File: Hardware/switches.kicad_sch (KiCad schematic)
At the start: 40 parts, among them J5 Conn_01x02_Male, J6 Conn_01x08_Male, J7 FAN, J8 XT60PW-F, J9 Conn_01x02_Male, Q1 SQS141ELNW-T1_GE3, Q2 SQS141ELNW-T1_GE3, Q3 SI7635DP-T1-GE3, Q4 SI7635DP-T1-GE3, Q5 SSM3K15AMFV,L3F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

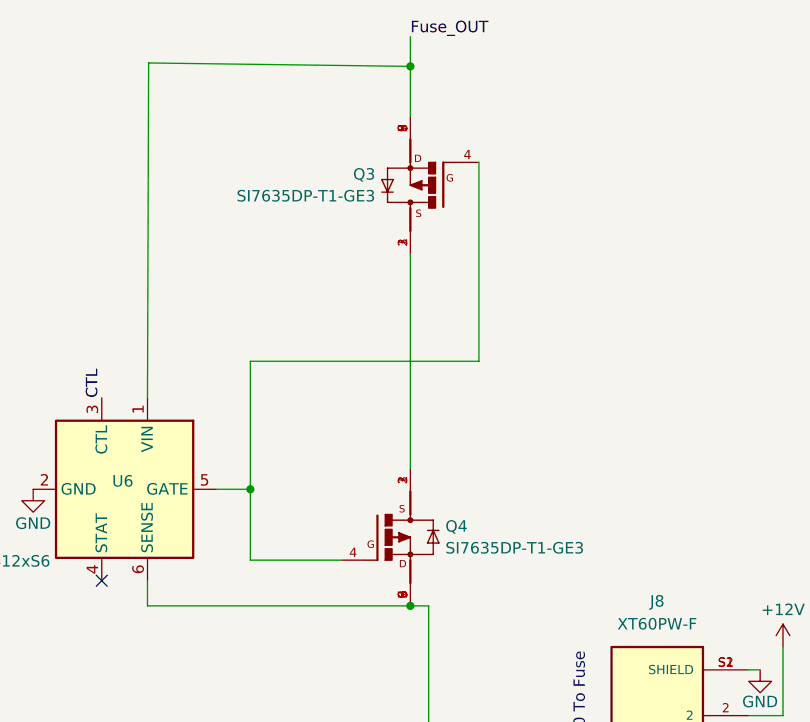
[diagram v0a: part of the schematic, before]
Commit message: feat: Changed mosfet to non deprecated version
Higher input voltage too: SI7135DP-T1-GE3
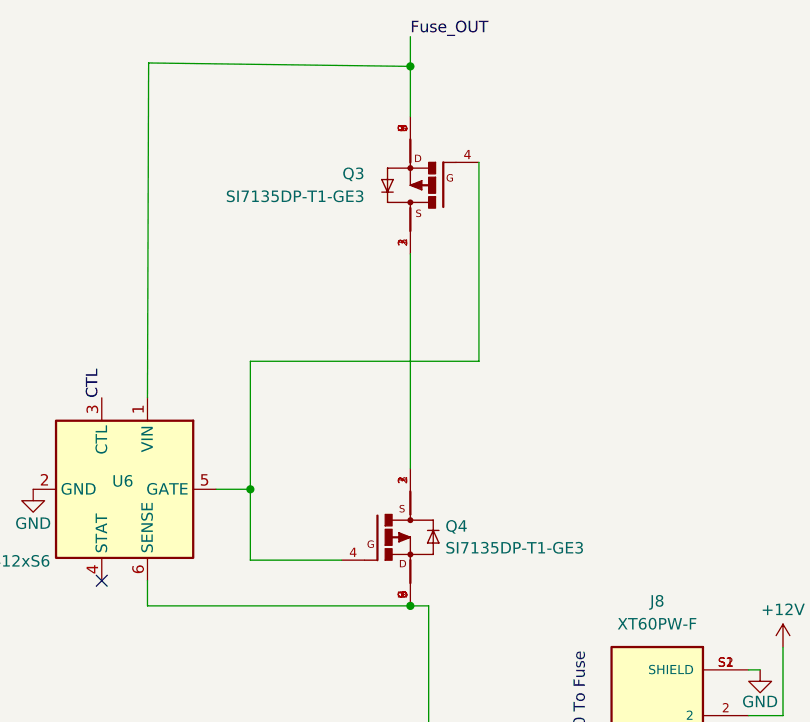
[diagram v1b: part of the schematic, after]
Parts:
- Q3, Q4: value SI7635DP-T1-GE3 -> SI7135DP-T1-GE3; Check_prices https://www.snapeda.com/parts/SI7635DP-T1-GE3/Vishay+Silico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 -> https://www.mouser.co.uk/ProductDetail/Vishay-Semiconductor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; Description_1 P-Channel 20 V 40A (Tc) 5W (Ta), 54W (Tc) Surface Mount Pow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 -> P-Channel 30 V 60A Surface Mount PowerPAK® SO-8; MP SI7635DP-T1-GE3 -> SI7135DP-T1-GE3; SnapEDA_Link https://www.snapeda.com/parts/SI7635DP-T1-GE3/Vishay+Silico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 -> (none)
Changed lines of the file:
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@@
 			)
 		)
-		(property "Value" "SI7635DP-T1-GE3"
+		(property "Value" "SI7135DP-T1-GE3"
 			(at 156.7942 85.5401 0)
 			(effects
@@
 			)
 		)
-		(property "Description_1" "\nP-Channel 20 V 40A (Tc) 5W (Ta), 54W (Tc) Surface Mount PowerPAK® SO-8\n"
+		(property "Description_1" "\nP-Channel 30 V 60A Surface Mount PowerPAK® SO-8\n"
 			(at 152.908 84.328 0)
 			(effects
@@
 			)
 		)
-		(property "Check_prices" "https://www.snapeda.com/parts/SI7635DP-T1-GE3/Vishay+Siliconix/view-part/?ref=eda"
+		(property "Check_prices" "https://www.mouser.co.uk/ProductDetail/Vishay-Semiconductors/SI7135DP-T1-GE3?qs=IRuQNBqMOcnMinMQAFe5cQ%3D%3D"
 			(at 152.908 84.328 0)
 			(effects
@@
 			)
 		)
-		(property "SnapEDA_Link" "https://www.snapeda.com/parts/SI7635DP-T1-GE3/Vishay+Siliconix/view-part/?ref=snap"
+		(property "SnapEDA_Link" ""
 			(at 152.908 84.328 0)
 			(effects
@@
 			)
 		)
-		(property "MP" "SI7635DP-T1-GE3"
+		(property "MP" "SI7135DP-T1-GE3"
 			(at 152.908 84.328 0)
 			(effects
@@
 	)
 	(symbol
-		(lib_id "iclr:SI7635DP-T1-GE3")
-		(at 152.908 45.212 180)
-		(unit 1)
-		(exclude_from_sim no)
-		(in_bom yes)
-		(on_board yes)
-		(dnp no)
-		(fields_autoplaced yes)
-		(property "Reference" "Q3"
-			(at 149.0219 43.9998 0)
-			(effects
-				(font
-					(size 1.27 1.27)
-				)
-				(justify left)
-			)
-		)
-		(property "Value" "SI7635DP-T1-GE3"
-			(at 149.0219 46.4241 0)
-			(effects
-				(font
-					(size 1.27 1.27)
-				)
-				(justify left)
-			)
-		)
-		(property "Footprint" "Package_SO:PowerPAK_SO-8_Single"
-			(at 152.908 45.212 0)
-			(effects
-				(font
-					(size 1.27 1.27)
-				)
-				(justify bottom)
-				(hide yes)
-			)
-		)
-		(property "Datasheet" ""
-			(at 152.908 45.212 0)
-			(effects
-				(font
-					(size 1.27 1.27)
-				)
-				(hide yes)
-			)
-		)
-		(property "Description" ""
-			(at 152.908 45.212 0)
-			(effects
-				(font
-					(size 1.27 1.27)
-				)
-				(hide yes)
-			)
-		)
-		(property "MF" "Vishay"
-			(at 152.908 45.212 0)
-			(effects
-				(font
-					(size 1.27 1.27)
-				)
-				(justify bottom)
-				(hide yes)
-			)
-		)
-		(property "Description_1" "\nP-Channel 20 V 40A (Tc) 5W (Ta), 54W (Tc) Surface Mount PowerPAK® SO-8\n"
-			(at 152.908 45.212 0)
-			(effects
-				(font
-					(size 1.27 1.27)
-				)
-				(justify bottom)
-				(hide yes)
-			)
-		)
-		(property "Package" "PowerPAK SO-8 Vishay"
-			(at 152.908 45.212 0)
-			(effects
-				(font
-					(size 1.27 1.27)
-				)
-				(justify bottom)
-				(hide yes)
-			)
-		)
-		(property "Price" "None"
-			(at 152.908 45.212 0)
-			(effects
-				(font
-					(size 1.27 1.27)
-				)
-				(justify bottom)
-				(hide yes)
-			)
-		)
-		(property "Check_prices" "https://www.snapeda.com/parts/SI7635DP-T1-GE3/Vishay+Siliconix/view-part/?ref=eda"
-			(at 152.908 45.212 0)
-			(effects
-				(font
-					(size 1.27 1.27)
-				)
-				(justify bottom)
-				(hide yes)
-			)
-		)
-		(property "SnapEDA_Link" "https://www.snapeda.com/parts/SI7635DP-T1-GE3/Vishay+Siliconix/view-part/?ref=snap"
-			(at 152.908 45.212 0)
-			(effects
-				(font
-					(size 1.27 1.27)
-				)
-				(justify bottom)
-				(hide yes)
-			)
-		)
-		(property "MP" "SI7635DP-T1-GE3"
-			(at 152.908 45.212 0)
-			(effects
-				(font
-					(size 1.27 1.27)
-				)
-				(justify bottom)
-				(hide yes)
-			)
-		)
-		(property "Availability" "In Stock"
-			(at 152.908 45.212 0)
-			(effects
-				(font
-					(size 1.27 1.27)
-				)
-				(justify bottom)
-				(hide yes)
-			)
-		)
-		(property "MANUFACTURER" "Vishay"
-			(at 152.908 45.212 0)
-			(effects
-				(font
-					(size 1.27 1.27)
-				)
-				(justify bottom)
-				(hide yes)
-			)
-		)
-		(pin "8"
-		)
-		(pin "2"
-		)
-		(pin "7"
-		)
-		(pin "4"
-		)
-		(pin "6"
-		)
-		(pin "9"
-		)
-		(pin "1"
-		)
-		(pin "3"
-		)
-		(pin "5"
-		)
-		(instances
-			(project "PDU"
-				(path "/e63e39d7-6ac0-4ffd-8aa3-1841a4541b55/133f56f4-a29c-4cbf-87b7-9d99a292e3c0"
-					(reference "Q3")
-					(unit 1)
-				)
-			)
-		)
-	)
-	(symbol
 		(lib_id "Device:Q_NMOS_GSD")
 		(at 242.316 39.878 0)
@@
 					(unit 1)
 				)
+			)
+		)
+	)
+	(symbol
+		(lib_id "iclr:SI7635DP-T1-GE3")
+		(at 152.908 45.212 180)
+		(unit 1)
+		(exclude_from_sim no)
+		(in_bom yes)
+		(on_board yes)
+		(dnp no)
+		(fields_autoplaced yes)
+		(property "Reference" "Q3"
+			(at 147.828 43.9419 0)
+			(effects
+				(font
+					(size 1.27 1.27)
+				)
+				(justify left)
+			)
+		)
+		(property "Value" "SI7135DP-T1-GE3"
+			(at 147.828 46.4819 0)
+			(effects
+				(font
+					(size 1.27 1.27)
+				)
+				(justify left)
+			)
+		)
+		(property "Footprint" "Package_SO:PowerPAK_SO-8_Single"
+			(at 152.908 45.212 0)
+			(effects
+				(font
+					(size 1.27 1.27)
+				)
+				(justify bottom)
+				(hide yes)
+			)
+		)
+		(property "Datasheet" ""
+			(at 152.908 45.212 0)
+			(effects
+				(font
+					(size 1.27 1.27)
+				)
+				(hide yes)
+			)
+		)
+		(property "Description" ""
+			(at 152.908 45.212 0)
+			(effects
+				(font
+					(size 1.27 1.27)
+				)
+				(hide yes)
+			)
+		)
+		(property "MF" "Vishay"
+			(at 152.908 45.212 0)
+			(effects
+				(font
+					(size 1.27 1.27)
+				)
+				(justify bottom)
+				(hide yes)
+			)
+		)
+		(property "Description_1" "\nP-Channel 30 V 60A Surface Mount PowerPAK® SO-8\n"
+			(at 152.908 45.212 0)
+			(effects
+				(font
+					(size 1.27 1.27)
+				)
+				(justify bottom)
+				(hide yes)
+			)
+		)
+		(property "Package" "PowerPAK SO-8 Vishay"
+			(at 152.908 45.212 0)
+			(effects
+				(font
+					(size 1.27 1.27)
+				)
+				(justify bottom)
+				(hide yes)
+			)
+		)
+		(property "Price" "None"
+			(at 152.908 45.212 0)
+			(effects
+				(font
+					(size 1.27 1.27)
+				)
+				(justify bottom)
+				(hide yes)
+			)
+		)
+		(property "Check_prices" "https://www.mouser.co.uk/ProductDetail/Vishay-Semiconductors/SI7135DP-T1-GE3?qs=IRuQNBqMOcnMinMQAFe5cQ%3D%3D"
+			(at 152.908 45.212 0)
+			(effects
+				(font
+					(size 1.27 1.27)
+				)
+				(justify bottom)
+				(hide yes)
+			)
+		)
+		(property "SnapEDA_Link" ""
+			(at 152.908 45.212 0)
+			(effects
+				(font
+					(size 1.27 1.27)
+				)
+				(justify bottom)
+				(hide yes)
+			)
+		)
+		(property "MP" "SI7135DP-T1-GE3"
+			(at 152.908 45.212 0)
+			(effects
+				(font
+					(size 1.27 1.27)
+				)
+				(justify bottom)
+				(hide yes)
+			)
+		)
+		(property "Availability" "In Stock"
+			(at 152.908 45.212 0)
+			(effects
+				(font
+					(size 1.27 1.27)
+				)
+				(justify bottom)
+				(hide yes)
+			)
+		)
+		(property "MANUFACTURER" "Vishay"
+			(at 152.908 45.212 0)
+			(effects
+				(font
+					(size 1.27 1.27)
+				)
+				(justify bottom)
+				(hide yes)
+			)
+		)
+		(pin "8"
+		)
+		(pin "2"
+		)
+		(pin "7"
+		)
+		(pin "4"
+		)
+		(pin "6"
+		)
+		(pin "9"
+		)
+		(pin "1"
+		)
+		(pin "3"
+		)
+		(pin "5"
+		)
+		(instances
+			(project "PDU"
+				(path "/e63e39d7-6ac0-4ffd-8aa3-1841a4541b55/133f56f4-a29c-4cbf-87b7-9d99a292e3c0"
+					(reference "Q3")
+					(unit 1)
+				)
